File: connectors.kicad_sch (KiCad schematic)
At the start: 12 parts, among them J1 RCJ-017, J2 USB4105-GF-A-120, J3 Conn_01x02_Pin, J4 Conn_01x02_Pin

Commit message: Reannotated schematic + restarted layout
woohoo
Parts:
- renumbered D5 to D3
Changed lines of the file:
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@@
 		(dnp no)
 		(fields_autoplaced yes)
-		(property "Reference" "D5"
+		(property "Reference" "D3"
 			(at 110.49 104.1399 0)
 			(effects
@@
 			(project ""
 				(path "/d9e790b9-8aa4-4e58-8bd7-6ef4bc890627/ed99070c-0835-415c-8078-0f260c71dd6d"
-					(reference "D5")
+					(reference "D3")
 					(unit 1)
 				)
@@
 		(dnp no)
 		(fields_autoplaced yes)
-		(property "Reference" "#PWR08"
+		(property "Reference" "#PWR07"
 			(at 72.39 127 0)
 			(effects
@@
 			(project "BinauralMic"
 				(path "/d9e790b9-8aa4-4e58-8bd7-6ef4bc890627/ed99070c-0835-415c-8078-0f260c71dd6d"
-					(reference "#PWR08")
+					(reference "#PWR07")
 					(unit 1)
 				)

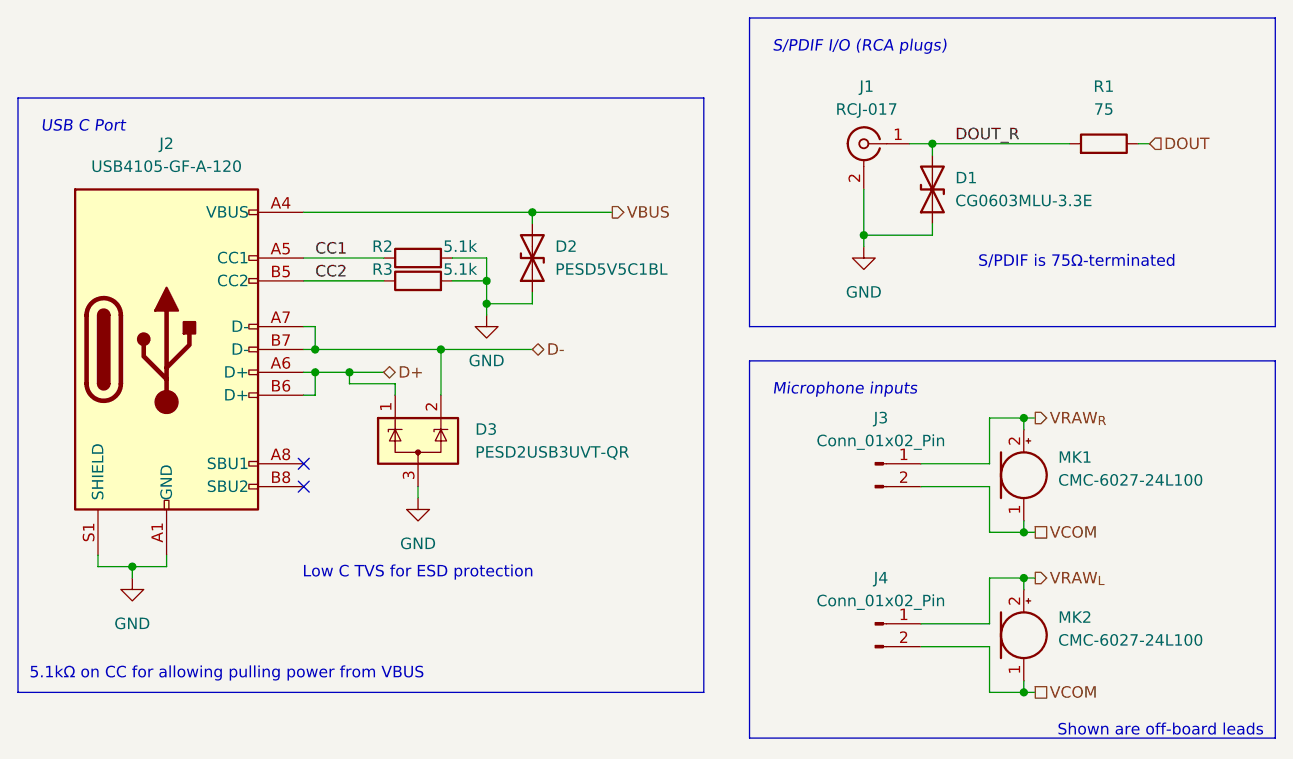
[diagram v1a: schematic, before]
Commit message: Add more detailed RCJ-014 model + shifting things around
Also added another ESD diode for VBUS because only one will be connected for USB C :/
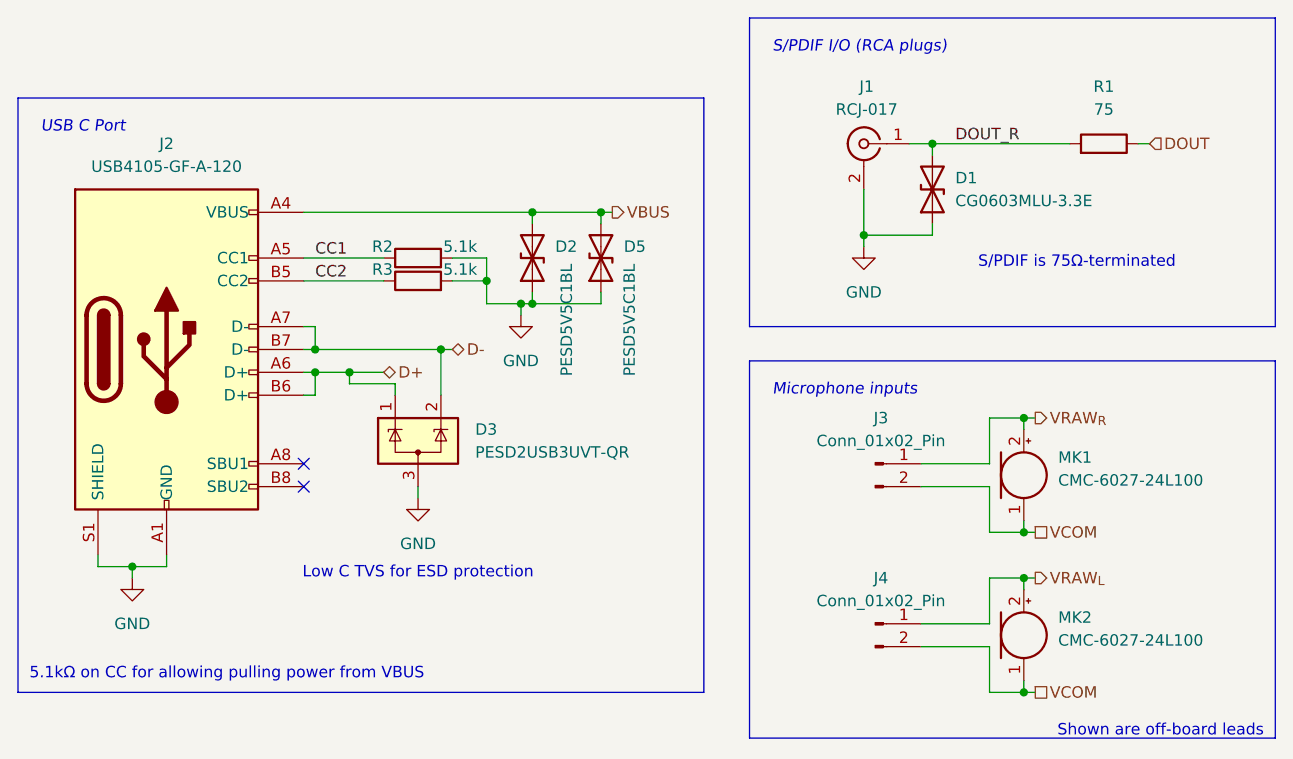
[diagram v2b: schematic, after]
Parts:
- added D5: PESD5V5C1BL, Diode_SMD:D_SOD-882, symbol Device:D_TVS
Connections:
- net GND: now also D5.1 (A1)
- net VBUS: now also D5.2 (A2)
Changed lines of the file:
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@@
+	)
+	(junction
+		(at 124.46 80.01)
+		(diameter 0)
+		(color 0 0 0 0)
 	)
 	(junction
@@
 	)
 	(junction
-		(at 111.76 90.17)
+		(at 171.45 115.57)
 		(diameter 0)
 		(color 0 0 0 0)
 	)
 	(junction
-		(at 171.45 115.57)
+		(at 116.84 90.17)
+		(diameter 0)
+		(color 0 0 0 0)
+	)
+	(junction
+		(at 115.57 90.17)
 		(diameter 0)
 		(color 0 0 0 0)
@@
 	(wire
 		(pts
+			(xy 115.57 90.17) (xy 111.76 90.17)
+		)
+		(stroke
+			(width 0)
+			(type default)
+		)
+	)
+	(wire
+		(pts
 			(xy 171.45 120.65) (xy 172.72 120.65)
 		)
@@
 	(wire
 		(pts
-			(xy 125.73 80.01) (xy 116.84 80.01)
+			(xy 125.73 80.01) (xy 124.46 80.01)
 		)
 		(stroke
@@
 	(wire
 		(pts
+			(xy 124.46 80.01) (xy 116.84 80.01)
+		)
+		(stroke
+			(width 0)
+			(type default)
+		)
+	)
+	(wire
+		(pts
 			(xy 153.67 77.47) (xy 153.67 82.55)
 		)
@@
 	(wire
 		(pts
-			(xy 111.76 90.17) (xy 111.76 91.44)
+			(xy 115.57 90.17) (xy 115.57 91.44)
 		)
 		(stroke
@@
 	(wire
 		(pts
+			(xy 124.46 88.9) (xy 124.46 90.17)
+		)
+		(stroke
+			(width 0)
+			(type default)
+		)
+	)
+	(wire
+		(pts
 			(xy 76.2 119.38) (xy 76.2 118.11)
 		)
@@
 	(wire
 		(pts
+			(xy 124.46 80.01) (xy 124.46 81.28)
+		)
+		(stroke
+			(width 0)
+			(type default)
+		)
+	)
+	(wire
+		(pts
+			(xy 116.84 90.17) (xy 115.57 90.17)
+		)
+		(stroke
+			(width 0)
+			(type default)
+		)
+	)
+	(wire
+		(pts
 			(xy 171.45 133.35) (xy 167.64 133.35)
 		)
@@
 	(wire
 		(pts
-			(xy 106.68 95.25) (xy 116.84 95.25)
+			(xy 106.68 95.25) (xy 107.95 95.25)
 		)
 		(stroke
@@
 	(wire
 		(pts
+			(xy 124.46 90.17) (xy 116.84 90.17)
+		)
+		(stroke
+			(width 0)
+			(type default)
+		)
+	)
+	(wire
+		(pts
 			(xy 167.64 102.87) (xy 171.45 102.87)
 		)
@@
 		(pts
 			(xy 106.68 95.25) (xy 106.68 100.33)
-		)
-		(stroke
-			(width 0)
-			(type default)
-		)
-	)
-	(wire
-		(pts
-			(xy 111.76 90.17) (xy 116.84 90.17)
 		)
 		(stroke
@@
 	(hierarchical_label "D-"
 		(shape bidirectional)
-		(at 116.84 95.25 0)
+		(at 107.95 95.25 0)
 		(fields_autoplaced yes)
 		(effects
@@
 	)
 	(symbol
-		(lib_id "power:GND")
-		(at 111.76 91.44 0)
+		(lib_id "Device:D_TVS")
+		(at 124.46 85.09 90)
 		(unit 1)
 		(exclude_from_sim no)
@@
 		(on_board yes)
 		(dnp no)
+		(property "Reference" "D5"
+			(at 127 83.8199 90)
+			(effects
+				(font
+					(size 1.27 1.27)
+				)
+				(justify right)
+			)
+		)
+		(property "Value" "PESD5V5C1BL"
+			(at 127.635 85.725 0)
+			(effects
+				(font
+					(size 1.27 1.27)
+				)
+				(justify right)
+			)
+		)
+		(property "Footprint" "Diode_SMD:D_SOD-882"
+			(at 124.46 85.09 0)
+			(effects
+				(font
+					(size 1.27 1.27)
+				)
+				(hide yes)
+			)
+		)
+		(property "Datasheet" "https://www.mouser.com/datasheet/2/916/PESD5V5C1BL-3162447.pdf"
+			(at 124.46 85.09 0)
+			(effects
+				(font
+					(size 1.27 1.27)
+				)
+				(hide yes)
+			)
+		)
+		(property "Description" "Bidirectional transient-voltage-suppression diode"
+			(at 124.46 85.09 0)
+			(effects
+				(font
+					(size 1.27 1.27)
+				)
+				(hide yes)
+			)
+		)
+		(property "Mouser Part Number" "771-PESD5V5C1BLYL "
+			(at 124.46 85.09 90)
+			(effects
+				(font
+					(size 1.27 1.27)
+				)
+				(hide yes)
+			)
+		)
+		(pin "2"
+		)
+		(pin "1"
+		)
+		(instances
+			(project "BinauralMic"
+				(path "/d9e790b9-8aa4-4e58-8bd7-6ef4bc890627/ed99070c-0835-415c-8078-0f260c71dd6d"
+					(reference "D5")
+					(unit 1)
+				)
+			)
+		)
+	)
+	(symbol
+		(lib_id "power:GND")
+		(at 115.57 91.44 0)
+		(unit 1)
+		(exclude_from_sim no)
+		(in_bom yes)
+		(on_board yes)
+		(dnp no)
 		(fields_autoplaced yes)
 		(property "Reference" "#PWR05"
-			(at 111.76 97.79 0)
+			(at 115.57 97.79 0)
 			(effects
 				(font
@@
 		)
 		(property "Value" "GND"
-			(at 111.76 96.52 0)
+			(at 115.57 96.52 0)
 			(effects
 				(font
@@
 		)
 		(property "Footprint" ""
-			(at 111.76 91.44 0)
+			(at 115.57 91.44 0)
 			(effects
 				(font
@@
 		)
 		(property "Datasheet" ""
-			(at 111.76 91.44 0)
+			(at 115.57 91.44 0)
 			(effects
 				(font
@@
 		)
 		(property "Description" "Power symbol creates a global label with name \"GND\" , ground"
-			(at 111.76 91.44 0)
+			(at 115.57 91.44 0)
 			(effects
 				(font
@@
 		(on_board yes)
 		(dnp no)
-		(fields_autoplaced yes)
 		(property "Reference" "D2"
 			(at 119.38 83.8199 90)
@@
 		)
 		(property "Value" "PESD5V5C1BL"
-			(at 119.38 86.3599 90)
-			(effects
-				(font
+			(at 120.65 85.725 0)
+			(effects
+				(font

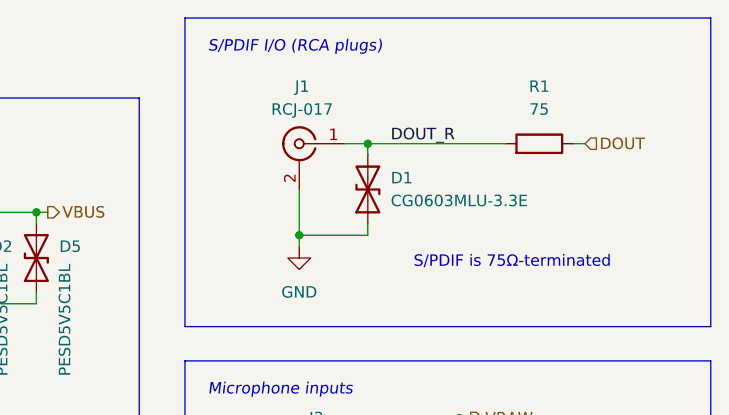
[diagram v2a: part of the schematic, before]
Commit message: Removed S/PIDF and still doing layout
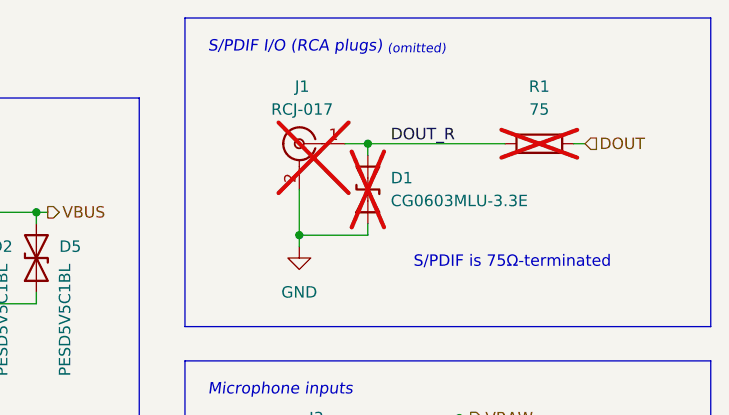
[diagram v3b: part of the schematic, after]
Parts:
- D1, J1, R1: now not fitted; now left out of the parts list
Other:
- note added: "S/PDIF I/O (RCA plugs) _{(omitted)}"
- note removed: "S/PDIF I/O (RCA plugs)"
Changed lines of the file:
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@@
 		)
 	)
-	(text "S/PDIF I/O (RCA plugs)"
+	(text "S/PDIF I/O (RCA plugs) _{(omitted)}"
 		(exclude_from_sim no)
 		(at 143.51 60.96 0)
@@
 		(unit 1)
 		(exclude_from_sim no)
-		(in_bom yes)
-		(on_board yes)
-		(dnp no)
+		(in_bom no)
+		(on_board no)
+		(dnp yes)
 		(fields_autoplaced yes)
 		(property "Reference" "J1"
@@
 		(unit 1)
 		(exclude_from_sim no)
-		(in_bom yes)
-		(on_board yes)
-		(dnp no)
+		(in_bom no)
+		(on_board no)
+		(dnp yes)
 		(fields_autoplaced yes)
 		(property "Reference" "D1"
@@
 		(unit 1)
 		(exclude_from_sim no)
-		(in_bom yes)
-		(on_board yes)
-		(dnp no)
+		(in_bom no)
+		(on_board no)
+		(dnp yes)
 		(fields_autoplaced yes)
 		(property "Reference" "R1"

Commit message: Ordered!
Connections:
- net GND: no longer J2.S1 (SHIELD)
- no-connect marks 2 -> 3
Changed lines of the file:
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@@
-	)
-	(junction
-		(at 72.39 119.38)
-		(diameter 0)
-		(color 0 0 0 0)
 	)
 	(junction
@@
 		(at 91.44 110.49)
 	)
+	(no_connect
+		(at 68.58 118.11)
+	)
 	(wire
 		(pts
@@
 	(wire
 		(pts
-			(xy 68.58 119.38) (xy 72.39 119.38)
-		)
-		(stroke
-			(width 0)
-			(type default)
-		)
-	)
-	(wire
-		(pts
 			(xy 91.44 95.25) (xy 92.71 95.25)
 		)
@@
 	(wire
 		(pts
-			(xy 76.2 119.38) (xy 76.2 118.11)
+			(xy 76.2 118.11) (xy 76.2 120.65)
 		)
 		(stroke
@@
 	(wire
 		(pts
-			(xy 72.39 119.38) (xy 76.2 119.38)
-		)
-		(stroke
-			(width 0)
-			(type default)
-		)
-	)
-	(wire
-		(pts
 			(xy 101.6 99.06) (xy 101.6 100.33)
 		)
@@
 	(wire
 		(pts
-			(xy 68.58 118.11) (xy 68.58 119.38)
-		)
-		(stroke
-			(width 0)
-			(type default)
-		)
-	)
-	(wire
-		(pts
 			(xy 91.44 97.79) (xy 92.71 97.79)
 		)
@@
 		(pts
 			(xy 167.64 120.65) (xy 171.45 120.65)
-		)
-		(stroke
-			(width 0)
-			(type default)
-		)
-	)
-	(wire
-		(pts
-			(xy 72.39 119.38) (xy 72.39 120.65)
 		)
 		(stroke
@@
 	(symbol
 		(lib_id "power:GND")
-		(at 72.39 120.65 0)
+		(at 76.2 120.65 0)
 		(unit 1)
 		(exclude_from_sim no)
@@
 		(fields_autoplaced yes)
 		(property "Reference" "#PWR07"
-			(at 72.39 127 0)
+			(at 76.2 127 0)
 			(effects
 				(font
@@
 		)
 		(property "Value" "GND"
-			(at 72.39 125.73 0)
+			(at 76.2 125.73 0)
 			(effects
 				(font
@@
 		)
 		(property "Footprint" ""
-			(at 72.39 120.65 0)
+			(at 76.2 120.65 0)
 			(effects
 				(font
@@
 		)
 		(property "Datasheet" ""
-			(at 72.39 120.65 0)
+			(at 76.2 120.65 0)
 			(effects
 				(font
@@
 		)
 		(property "Description" "Power symbol creates a global label with name \"GND\" , ground"
-			(at 72.39 120.65 0)
-			(effects
-				(font
+			(at 76.2 120.65 0)
+			(effects
+				(font
